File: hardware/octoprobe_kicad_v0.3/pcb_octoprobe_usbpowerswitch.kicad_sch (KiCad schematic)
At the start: 4 parts, among them U1201 MT9700

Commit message: PCB: Oscillator
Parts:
- R1201: footprint Resistor_SMD:R_0402_1005Metric -> Resistor_SMD:R_0805_2012Metric
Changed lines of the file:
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@@
 			)
 		)
-		(property "Footprint" "Resistor_SMD:R_0402_1005Metric"
+		(property "Footprint" "Resistor_SMD:R_0805_2012Metric"
 			(at 81.788 90.17 90)
 			(effects

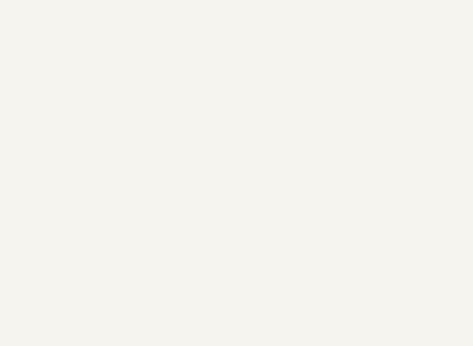
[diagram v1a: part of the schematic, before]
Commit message: PCB: Add "Open Hardware"
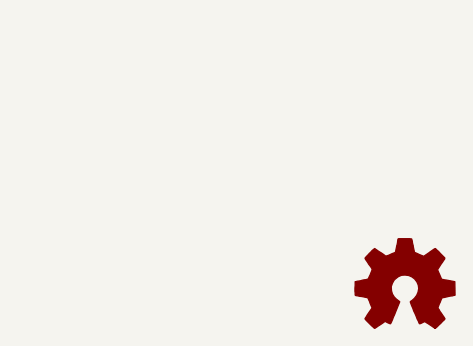
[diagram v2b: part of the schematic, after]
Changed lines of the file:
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@@
+	)
+	(symbol
+		(lib_id "Graphic:Logo_Open_Hardware_Small")
+		(at 275.59 173.99 0)
+		(unit 1)
+		(exclude_from_sim yes)
+		(in_bom no)
+		(on_board no)
+		(dnp no)
+		(fields_autoplaced yes)
+		(property "Reference" "#SYM1401"
+			(at 275.59 167.005 0)
+			(effects
+				(font
+					(size 1.27 1.27)
+				)
+				(hide yes)
+			)
+		)
+		(property "Value" "Logo_Open_Hardware_Small"
+			(at 275.59 179.705 0)
+			(effects
+				(font
+					(size 1.27 1.27)
+				)
+				(hide yes)
+			)
+		)
+		(property "Footprint" ""
+			(at 275.59 173.99 0)
+			(effects
+				(font
+					(size 1.27 1.27)
+				)
+				(hide yes)
+			)
+		)
+		(property "Datasheet" "~"
+			(at 275.59 173.99 0)
+			(effects
+				(font
+					(size 1.27 1.27)
+				)
+				(hide yes)
+			)
+		)
+		(property "Description" "Open Hardware logo, small"
+			(at 275.59 173.99 0)
+			(effects
+				(font
+					(size 1.27 1.27)
+				)
+				(hide yes)
+			)
+		)
+		(instances
+			(project "pcb_octoprobe"
+				(path "/35c47459-45a7-4753-acae-c8b47e7575e1/5d792043-9bfa-4fa6-be3c-ff15d7bc02be"
+					(reference "#SYM1401")
+					(unit 1)
+				)
+				(path "/35c47459-45a7-4753-acae-c8b47e7575e1/9cc2153c-44b9-4e7f-8961-835664992a07"
+					(reference "#SYM401")
+					(unit 1)
+				)
+			)
+		)
 	)
 	(symbol

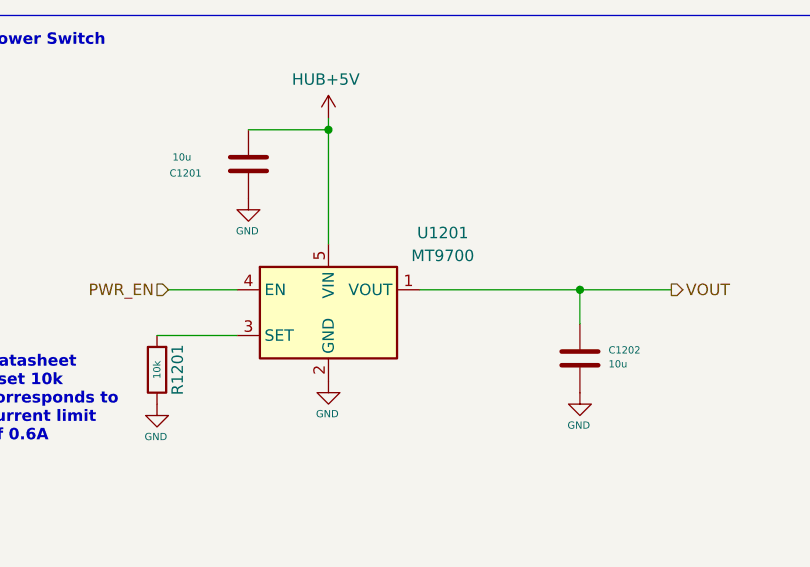
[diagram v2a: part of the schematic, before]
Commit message: PCB: Production files ready
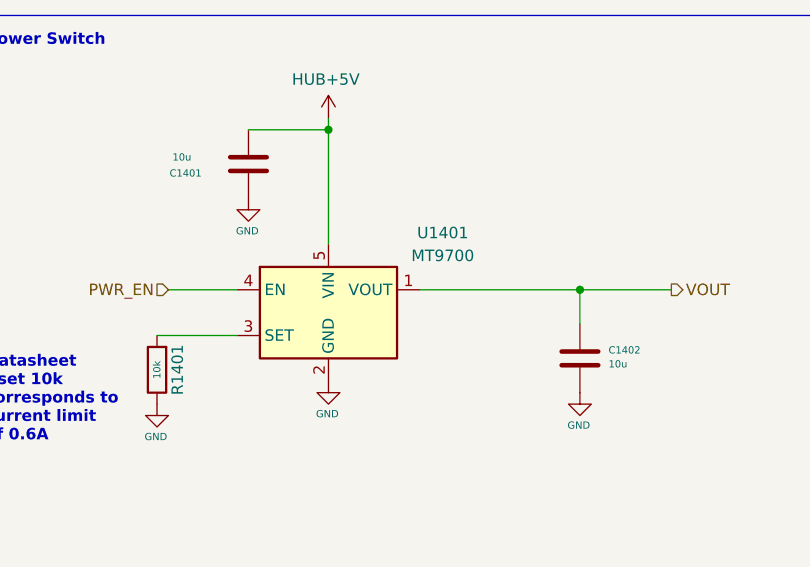
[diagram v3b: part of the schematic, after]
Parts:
- renumbered C1201 to C1401, C1202 to C1402, R1201 to R1401, U1201 to U1401
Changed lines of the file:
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@@
 	(title_block
 		(title "Octoprobe tentacle")
-		(date "2024-07-31")
+		(date "2024-08-04")
 		(rev "0.3")
 		(company "Hans Märki, Märki Informatik")
@@
 		(on_board yes)
 		(dnp no)
-		(property "Reference" "C1202"
+		(property "Reference" "C1402"
 			(at 130.175 87.9856 0)
 			(effects
@@
 			(project "pcb_octoprobe"
 				(path "/35c47459-45a7-4753-acae-c8b47e7575e1/5d792043-9bfa-4fa6-be3c-ff15d7bc02be"
-					(reference "C1202")
-					(unit 1)
-				)
-				(path "/35c47459-45a7-4753-acae-c8b47e7575e1/9cc2153c-44b9-4e7f-8961-835664992a07"
-					(reference "C902")
+					(reference "C1402")
+					(unit 1)
+				)
+				(path "/35c47459-45a7-4753-acae-c8b47e7575e1/9cc2153c-44b9-4e7f-8961-835664992a07"
+					(reference "C402")
 					(unit 1)
 				)
@@
 		(on_board yes)
 		(dnp no)
-		(property "Reference" "#PWR01204"
+		(property "Reference" "#PWR01404"
 			(at 99.06 97.79 0)
 			(effects
@@
 			(project "pcb_octoprobe"
 				(path "/35c47459-45a7-4753-acae-c8b47e7575e1/5d792043-9bfa-4fa6-be3c-ff15d7bc02be"
-					(reference "#PWR01204")
-					(unit 1)
-				)
-				(path "/35c47459-45a7-4753-acae-c8b47e7575e1/9cc2153c-44b9-4e7f-8961-835664992a07"
-					(reference "#PWR0904")
+					(reference "#PWR01404")
+					(unit 1)
+				)
+				(path "/35c47459-45a7-4753-acae-c8b47e7575e1/9cc2153c-44b9-4e7f-8961-835664992a07"
+					(reference "#PWR0404")
 					(unit 1)
 				)
@@
 		(on_board yes)
 		(dnp no)
-		(property "Reference" "#PWR01202"
+		(property "Reference" "#PWR01402"
 			(at 90.17 77.47 0)
 			(effects
@@
 			(project "pcb_octoprobe"
 				(path "/35c47459-45a7-4753-acae-c8b47e7575e1/5d792043-9bfa-4fa6-be3c-ff15d7bc02be"
-					(reference "#PWR01202")
-					(unit 1)
-				)
-				(path "/35c47459-45a7-4753-acae-c8b47e7575e1/9cc2153c-44b9-4e7f-8961-835664992a07"
-					(reference "#PWR0902")
+					(reference "#PWR01402")
+					(unit 1)
+				)
+				(path "/35c47459-45a7-4753-acae-c8b47e7575e1/9cc2153c-44b9-4e7f-8961-835664992a07"
+					(reference "#PWR0402")
 					(unit 1)
 				)
@@
 		(on_board yes)
 		(dnp no)
-		(property "Reference" "#PWR01201"
+		(property "Reference" "#PWR01401"
 			(at 80.01 100.33 0)
 			(effects
@@
 			(project "pcb_octoprobe"
 				(path "/35c47459-45a7-4753-acae-c8b47e7575e1/5d792043-9bfa-4fa6-be3c-ff15d7bc02be"
-					(reference "#PWR01201")
-					(unit 1)
-				)
-				(path "/35c47459-45a7-4753-acae-c8b47e7575e1/9cc2153c-44b9-4e7f-8961-835664992a07"
-					(reference "#PWR0901")
+					(reference "#PWR01401")
+					(unit 1)
+				)
+				(path "/35c47459-45a7-4753-acae-c8b47e7575e1/9cc2153c-44b9-4e7f-8961-835664992a07"
+					(reference "#PWR0401")
 					(unit 1)
 				)
@@
 		(on_board yes)
 		(dnp no)
-		(property "Reference" "#PWR01203"
+		(property "Reference" "#PWR01403"
 			(at 99.06 66.04 0)
 			(effects
@@
 			(project "pcb_octoprobe"
 				(path "/35c47459-45a7-4753-acae-c8b47e7575e1/5d792043-9bfa-4fa6-be3c-ff15d7bc02be"
-					(reference "#PWR01203")
-					(unit 1)
-				)
-				(path "/35c47459-45a7-4753-acae-c8b47e7575e1/9cc2153c-44b9-4e7f-8961-835664992a07"
-					(reference "#PWR0903")
+					(reference "#PWR01403")
+					(unit 1)
+				)
+				(path "/35c47459-45a7-4753-acae-c8b47e7575e1/9cc2153c-44b9-4e7f-8961-835664992a07"
+					(reference "#PWR0403")
 					(unit 1)
 				)
@@
 		(dnp no)
 		(fields_autoplaced yes)
-		(property "Reference" "U1201"
+		(property "Reference" "U1401"
 			(at 111.76 74.9614 0)
 			(effects
@@
 			(project "pcb_octoprobe"
 				(path "/35c47459-45a7-4753-acae-c8b47e7575e1/5d792043-9bfa-4fa6-be3c-ff15d7bc02be"
-					(reference "U1201")
-					(unit 1)
-				)
-				(path "/35c47459-45a7-4753-acae-c8b47e7575e1/9cc2153c-44b9-4e7f-8961-835664992a07"
-					(reference "U901")
+					(reference "U1401")
+					(unit 1)
+				)
+				(path "/35c47459-45a7-4753-acae-c8b47e7575e1/9cc2153c-44b9-4e7f-8961-835664992a07"
+					(reference "U401")
 					(unit 1)
 				)
@@
 		(on_board yes)
 		(dnp no)
-		(property "Reference" "#PWR01205"
+		(property "Reference" "#PWR01405"
 			(at 127 99.06 0)
 			(effects
@@
 			(project "pcb_octoprobe"
 				(path "/35c47459-45a7-4753-acae-c8b47e7575e1/5d792043-9bfa-4fa6-be3c-ff15d7bc02be"
-					(reference "#PWR01205")
-					(unit 1)
-				)
-				(path "/35c47459-45a7-4753-acae-c8b47e7575e1/9cc2153c-44b9-4e7f-8961-835664992a07"
-					(reference "#PWR0905")
+					(reference "#PWR01405")
+					(unit 1)
+				)
+				(path "/35c47459-45a7-4753-acae-c8b47e7575e1/9cc2153c-44b9-4e7f-8961-835664992a07"
+					(reference "#PWR0405")
 					(unit 1)
 				)
@@
 		(on_board yes)
 		(dnp no)
-		(property "Reference" "C1201"
+		(property "Reference" "C1401"
 			(at 84.963 68.326 0)
 			(effects
@@
 			(project "pcb_octoprobe"
 				(path "/35c47459-45a7-4753-acae-c8b47e7575e1/5d792043-9bfa-4fa6-be3c-ff15d7bc02be"
-					(reference "C1201")
-					(unit 1)
-				)
-				(path "/35c47459-45a7-4753-acae-c8b47e7575e1/9cc2153c-44b9-4e7f-8961-835664992a07"
-					(reference "C901")
+					(reference "C1401")
+					(unit 1)
+				)
+				(path "/35c47459-45a7-4753-acae-c8b47e7575e1/9cc2153c-44b9-4e7f-8961-835664992a07"
+					(reference "C401")
 					(unit 1)
 				)
@@
 		(on_board yes)
 		(dnp no)
-		(property "Reference" "R1201"
+		(property "Reference" "R1401"
 			(at 82.296 90.17 90)
 			(effects
@@
 			(project "pcb_octoprobe"
 				(path "/35c47459-45a7-4753-acae-c8b47e7575e1/5d792043-9bfa-4fa6-be3c-ff15d7bc02be"
-					(reference "R1201")
-					(unit 1)
-				)
-				(path "/35c47459-45a7-4753-acae-c8b47e7575e1/9cc2153c-44b9-4e7f-8961-835664992a07"
-					(reference "R901")
-					(unit 1)
-				)
+					(reference "R1401")
+					(unit 1)
+				)
+				(path "/35c47459-45a7-4753-acae-c8b47e7575e1/9cc2153c-44b9-4e7f-8961-835664992a07"
+					(reference "R401")
+					(unit 1)
+				)
